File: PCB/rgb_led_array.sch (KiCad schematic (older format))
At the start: 1 part

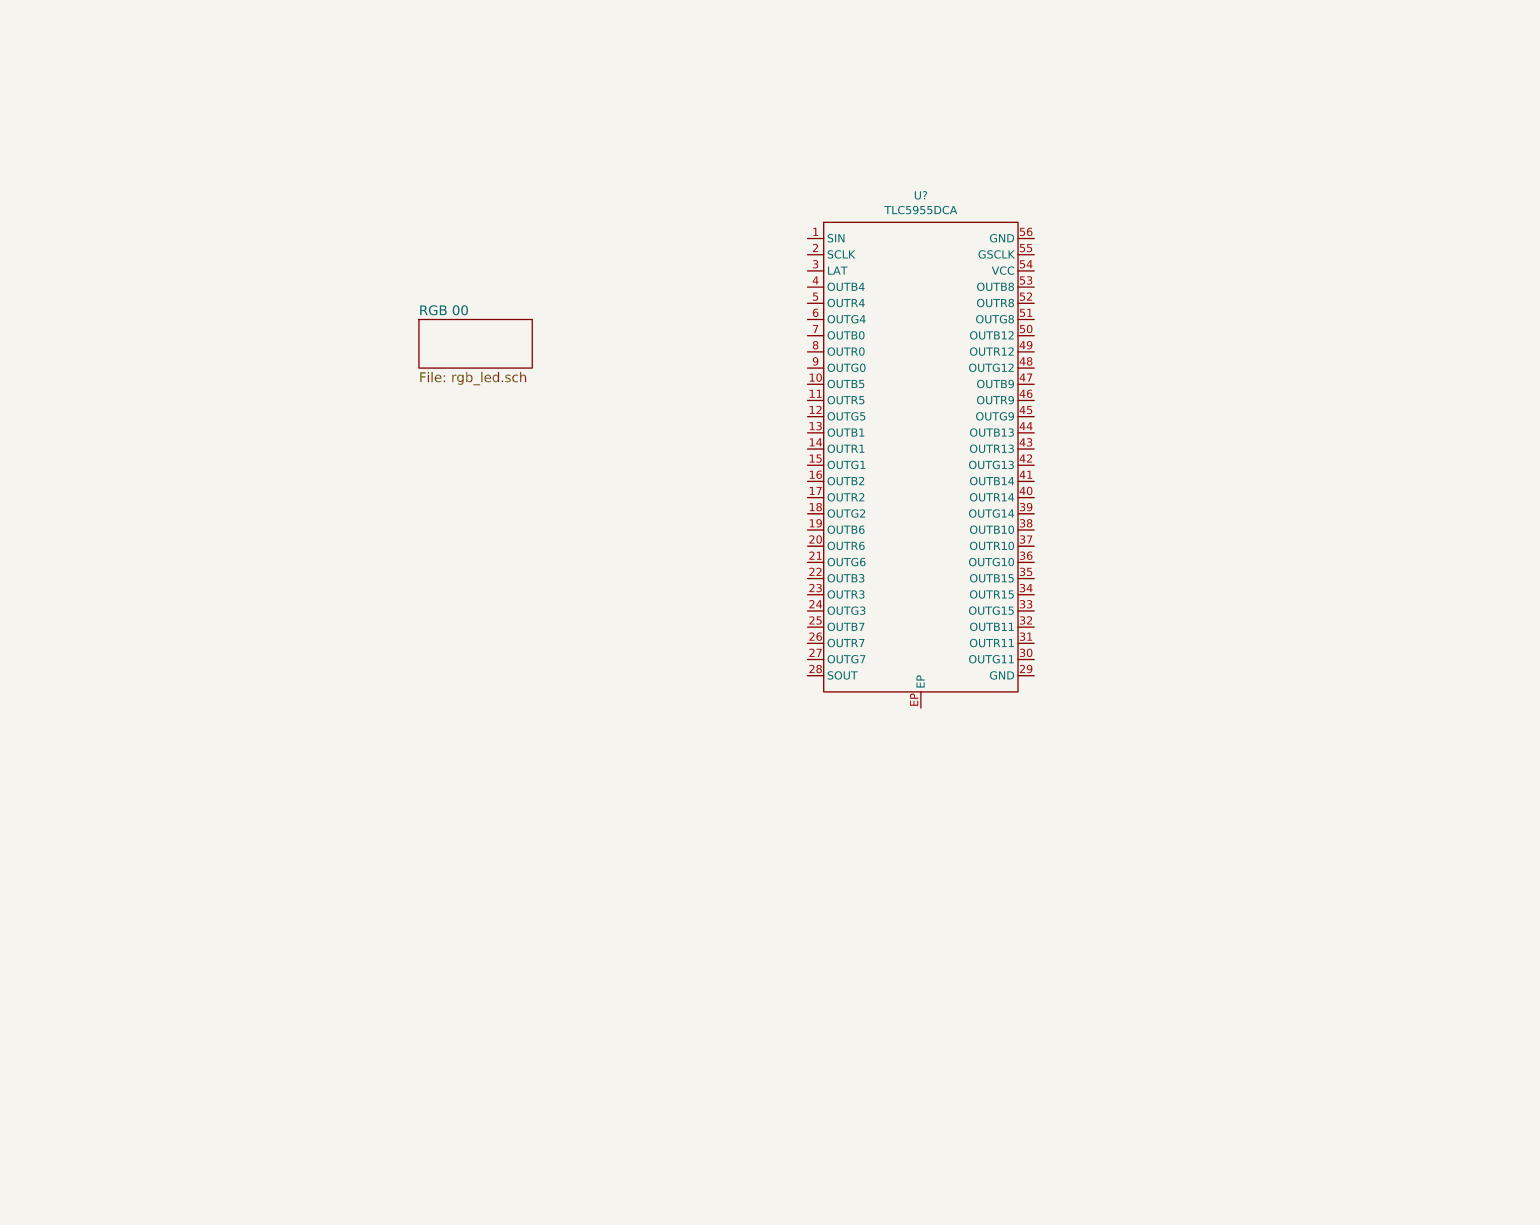
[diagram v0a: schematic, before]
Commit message: PCB Edge.Cuts Defined
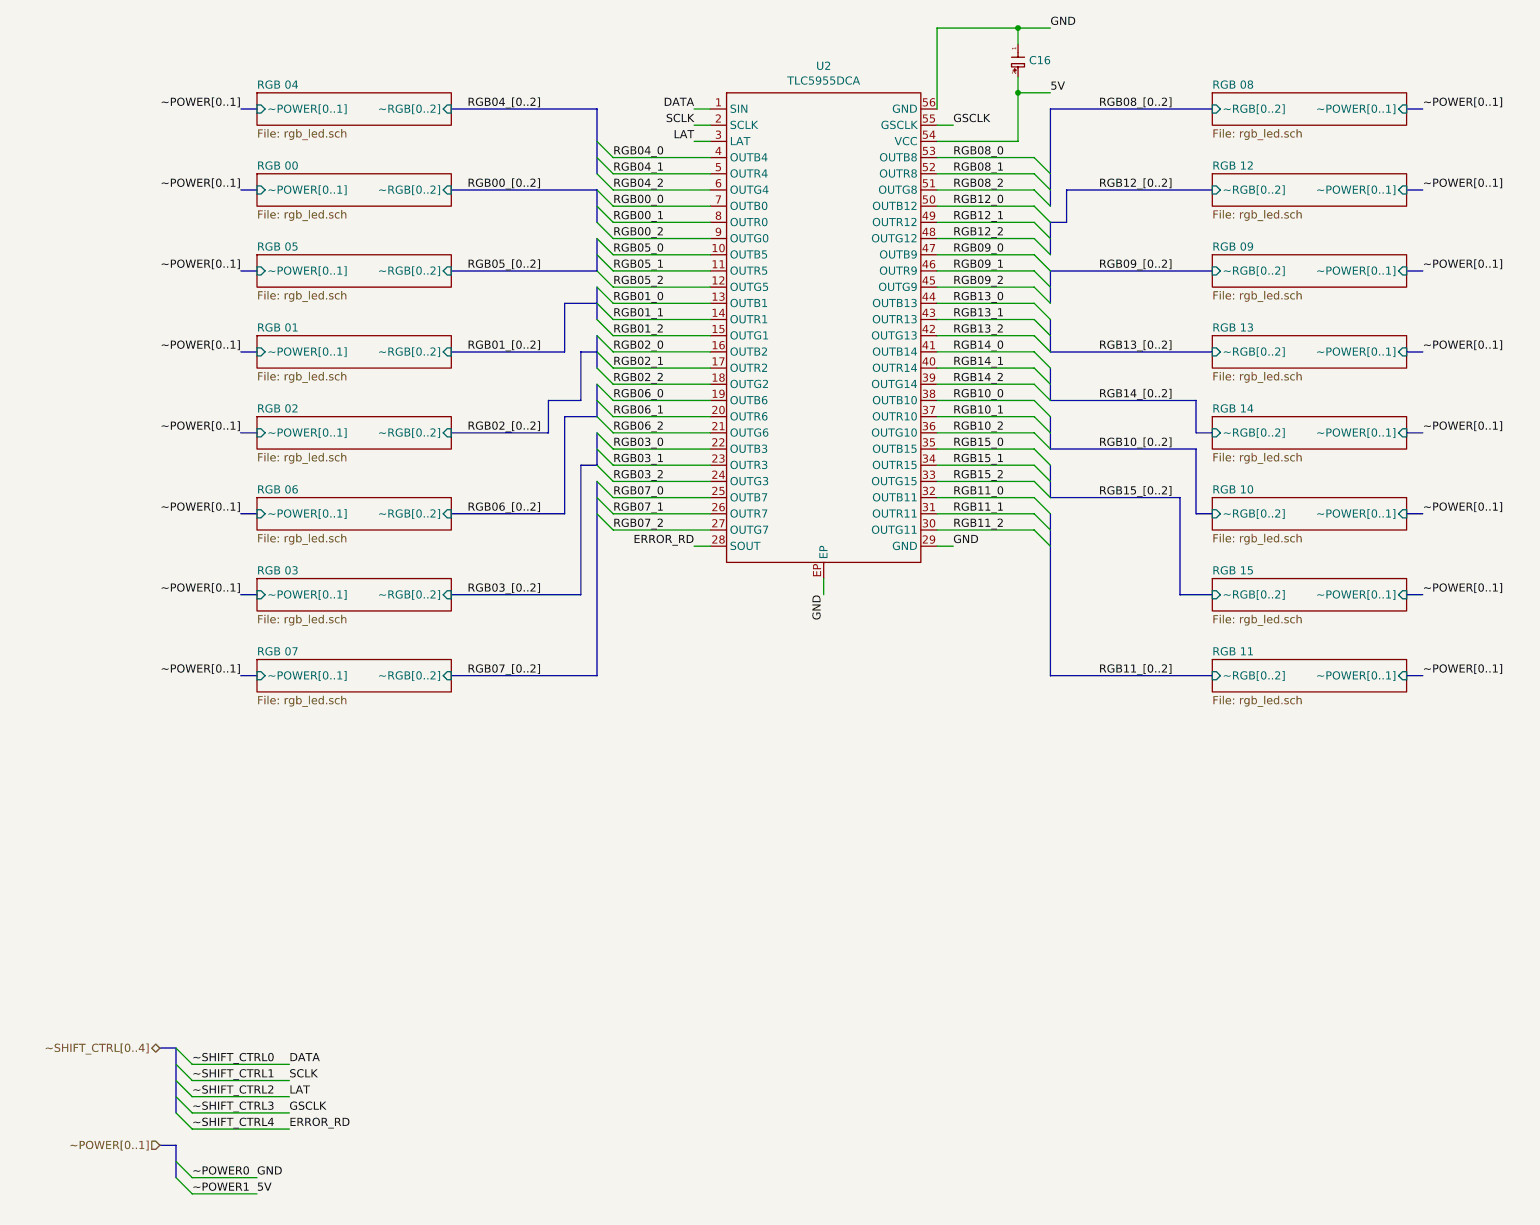
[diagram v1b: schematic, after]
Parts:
- added C16: Capacitor-Pol, local:SMD-POL-1206, symbol Capacitor-Pol
- U2: renamed from U?; footprint (none) -> local:HTSSOP-56_14x6.1; Description (none) -> LED Driver IC 48 Output Linear Analog Dimming 30mA 56-HTSSOP; Included in BOM (none) -> Yes; MPN (none) -> TLC5955DCAR
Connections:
- net DATA: now reaches U2.1 (SIN)
- net RGB05_0: now reaches U2.10 (OUTB5)
- net RGB05_1: now reaches U2.11 (OUTR5)
- net RGB05_2: now reaches U2.12 (OUTG5)
- net RGB01_0: now reaches U2.13 (OUTB1)
- net RGB01_1: now reaches U2.14 (OUTR1)
- net RGB01_2: now reaches U2.15 (OUTG1)
- net RGB02_0: now reaches U2.16 (OUTB2)
- net RGB02_1: now reaches U2.17 (OUTR2)
- net RGB02_2: now reaches U2.18 (OUTG2)
- net RGB06_0: now reaches U2.19 (OUTB6)
- net SCLK: now reaches U2.2 (SCLK)
- net RGB06_1: now reaches U2.20 (OUTR6)
- net RGB06_2: now reaches U2.21 (OUTG6)
- net RGB03_0: now reaches U2.22 (OUTB3)
- net RGB03_1: now reaches U2.23 (OUTR3)
- net RGB03_2: now reaches U2.24 (OUTG3)
- net RGB07_0: now reaches U2.25 (OUTB7)
- net RGB07_1: now reaches U2.26 (OUTR7)
- net RGB07_2: now reaches U2.27 (OUTG7)
- net ERROR_RD: now reaches U2.28 (SOUT)
- net GND: now reaches U2.29 (GND)
- net GND: now also U2.56 (GND), U2.EP, C16.1
- net LAT: now reaches U2.3 (LAT)
- net RGB11_2: now reaches U2.30 (OUTG11)
- net RGB11_1: now reaches U2.31 (OUTR11)
- net RGB11_0: now reaches U2.32 (OUTB11)
- net RGB15_2: now reaches U2.33 (OUTG15)
- net RGB15_1: now reaches U2.34 (OUTR15)
- net RGB15_0: now reaches U2.35 (OUTB15)
- net RGB10_2: now reaches U2.36 (OUTG10)
- net RGB10_1: now reaches U2.37 (OUTR10)
- net RGB10_0: now reaches U2.38 (OUTB10)
- net RGB14_2: now reaches U2.39 (OUTG14)
- net RGB04_0: now reaches U2.4 (OUTB4)
- net RGB14_1: now reaches U2.40 (OUTR14)
- net RGB14_0: now reaches U2.41 (OUTB14)
- net RGB13_2: now reaches U2.42 (OUTG13)
- net RGB13_1: now reaches U2.43 (OUTR13)
- net RGB13_0: now reaches U2.44 (OUTB13)
- net RGB09_2: now reaches U2.45 (OUTG9)
- net RGB09_1: now reaches U2.46 (OUTR9)
- net RGB09_0: now reaches U2.47 (OUTB9)
- net RGB12_2: now reaches U2.48 (OUTG12)
- net RGB12_1: now reaches U2.49 (OUTR12)
- net RGB04_1: now reaches U2.5 (OUTR4)
- net RGB12_0: now reaches U2.50 (OUTB12)
- net RGB08_2: now reaches U2.51 (OUTG8)
- net RGB08_1: now reaches U2.52 (OUTR8)
- net RGB08_0: now reaches U2.53 (OUTB8)
- net 5V: now reaches U2.54 (VCC)
- net 5V: now also C16.2
- net GSCLK: now reaches U2.55 (GSCLK)
- net RGB04_2: now reaches U2.6 (OUTG4)
- net RGB00_0: now reaches U2.7 (OUTB0)
- net RGB00_1: now reaches U2.8 (OUTR0)
- net RGB00_2: now reaches U2.9 (OUTG0)
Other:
- moved on the sheet: U2

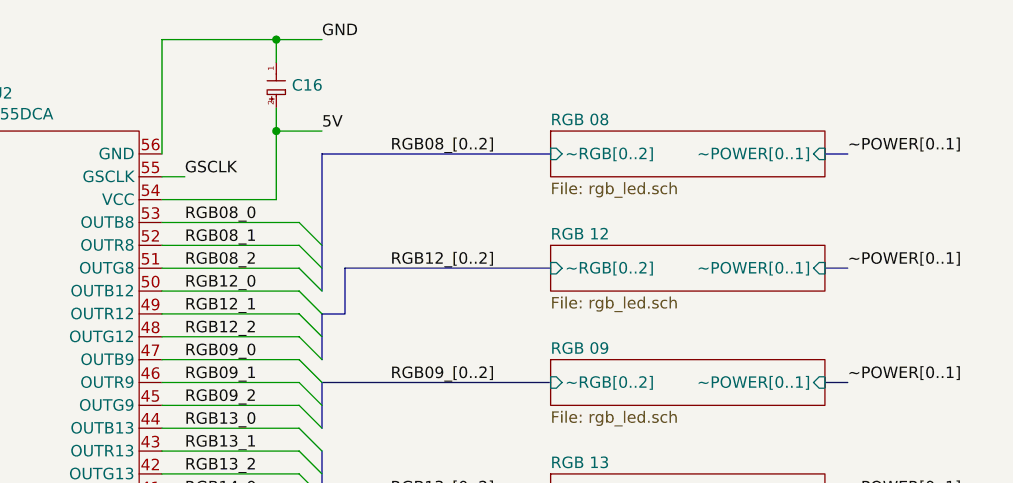
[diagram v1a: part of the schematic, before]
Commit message: Removed extra LED
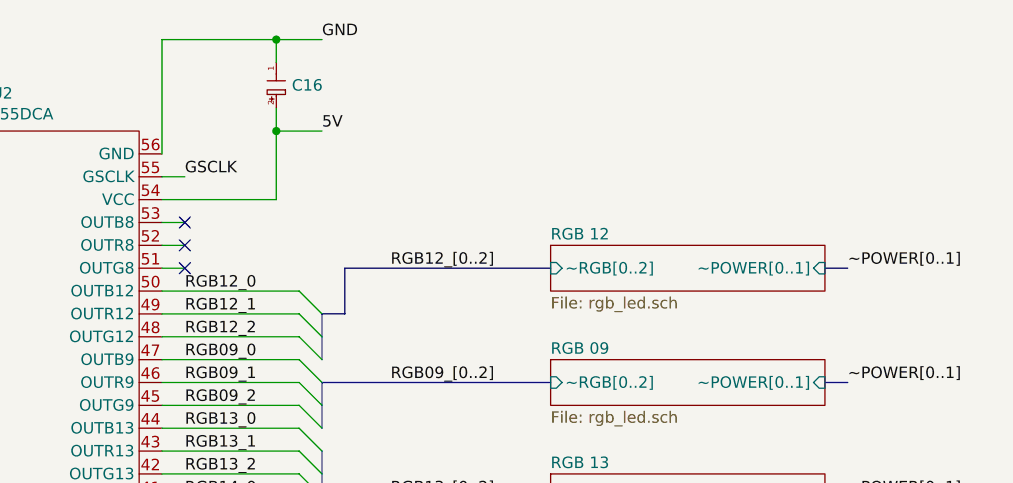
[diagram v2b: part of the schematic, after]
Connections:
- net RGB08_0: no longer names the net of U2.53 (OUTB8)
- net RGB08_1: no longer names the net of U2.52 (OUTR8)
- net RGB08_2: no longer names the net of U2.51 (OUTG8)
- no-connect marks 0 -> 3
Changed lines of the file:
@@
 $Descr A 11000 8500
 encoding utf-8
-Sheet 4 20
+Sheet 4 19
 Title "Christmas Tree Disco"
 Date "2017-08-01"
@@
 F2 "~~RGB[0..2]" I R 3100 4600 50
 F3 "~~POWER[0..1]" I L 1900 4600 50
-$EndSheet
-$Sheet
-S 7800 1000 1200 200
-U 59817080
-F0 "RGB 08" 50
-F1 "rgb_led.sch" 50
-F2 "~~RGB[0..2]" I L 7800 1100 50
-F3 "~~POWER[0..1]" I R 9000 1100 50
 $EndSheet
 Wire Bus Line
@@
 	6100 1900 6700 1900
 Wire Wire Line
-	6100 1400 6700 1400
-Wire Wire Line
-	6100 1500 6700 1500
-Wire Wire Line
-	6100 1600 6700 1600
-Wire Wire Line
 	6100 2000 6700 2000
 Wire Wire Line
@@
 	6100 3700 6700 3700
 Entry Wire Line
-	6700 1400 6800 1500
-Entry Wire Line
-	6700 1500 6800 1600
-Entry Wire Line
-	6700 1600 6800 1700
-Entry Wire Line
 	6700 1700 6800 1800
 Entry Wire Line
@@
 	6700 3700 6800 3800
 Wire Bus Line
-	6800 1100 6800 1700
-Wire Bus Line
 	6800 1800 6800 2000
 Wire Bus Line
@@
 Wire Bus Line
 	6800 3600 6800 4600
-Wire Bus Line
-	7800 1100 6800 1100
 $Sheet
 S 7800 1500 1200 200
@@
 Wire Bus Line
 	6800 4600 7800 4600
-Text Label 6200 1400 0    50   ~ 0
-RGB08_0
-Text Label 6200 1500 0    50   ~ 0
-RGB08_1
-Text Label 6200 1600 0    50   ~ 0
-RGB08_2
 Text Label 6200 1700 0    50   ~ 0
 RGB12_0
@@
 Text Label 6200 3700 0    50   ~ 0
 RGB11_2
-Text Label 7100 1100 0    50   ~ 0
-RGB08_[0..2]
 Text Label 7100 1600 0    50   ~ 0
 RGB12_[0..2]
@@
 Text Label 1800 1100 2    50   ~ 0
 ~~POWER[0..1]
-Text Label 9100 1100 0    50   ~ 0
-~~POWER[0..1]
 Text Label 9100 1600 0    50   ~ 0
 ~~POWER[0..1]
@@
 Wire Bus Line
 	9000 1600 9100 1600
-Wire Bus Line
-	9000 1100 9100 1100
+Wire Wire Line
+	6100 1400 6200 1400
+Wire Wire Line
+	6100 1500 6200 1500
+Wire Wire Line
+	6100 1600 6200 1600
+NoConn ~ 6200 1400
+NoConn ~ 6200 1500
+NoConn ~ 6200 1600
 $EndSCHEMATC

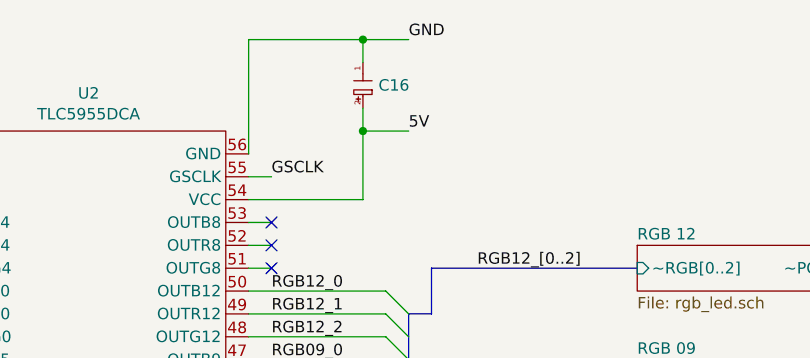
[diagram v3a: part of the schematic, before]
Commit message: PCB Layout
TODO: Change pinouts on dev kit to be compatable with Capacitive Touch
Audio booster pack.
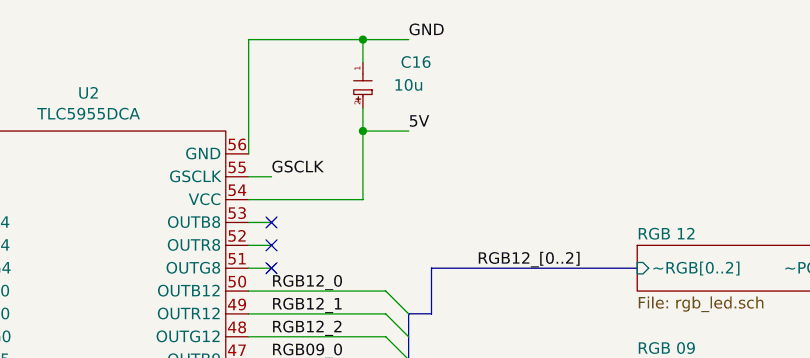
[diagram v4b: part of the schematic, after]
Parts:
- C16: value Capacitor-Pol -> 10u; Description ? -> CAP TANT 10UF 10V 10% 1206; MPN ? -> F931A106KAA
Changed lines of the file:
@@
 Text Label 7100 4600 0    50   ~ 0
 RGB11_[0..2]
-$Comp
-L Capacitor-Pol C16
-U 1 1 59833E85
-P 6600 800
-F 0 "C16" V 6600 868 50  0000 L CNN
-F 1 "Capacitor-Pol" H 6600 960 50  0001 C CNN
-F 2 "local:SMD-POL-1206" H 6600 800 60  0001 C CNN
-F 3 "" H 6600 800 60  0001 C CNN
-F 4 "?" H 6600 800 60  0001 C CNN "MPN"
-F 5 "?" H 6600 800 60  0001 C CNN "Description"
-F 6 "Yes" H 6600 800 60  0001 C CNN "Included in BOM"
-	1    6600 800
-	0    1    1    0
-$EndComp
 Wire Wire Line
 	6600 1300 6100 1300
@@
 NoConn ~ 6200 1500
 NoConn ~ 6200 1600
+$Comp
+L Capacitor-Pol C16
+U 1 1 59893C97
+P 6600 800
+F 0 "C16" V 6500 1100 50  0000 R CNN
+F 1 "10u" V 6600 1000 50  0000 C CNN
+F 2 "local:SMD-POL-1206" H 6600 800 60  0001 C CNN
+F 3 "http://datasheets.avx.com/F93.pdf" H 6600 800 60  0001 C CNN
+F 4 "F931A106KAA" H 6600 800 60  0001 C CNN "MPN"
+F 5 "CAP TANT 10UF 10V 10% 1206" H 6600 800 60  0001 C CNN "Description"
+F 6 "Yes" H 6600 800 60  0001 C CNN "Included in BOM"
+	1    6600 800
+	0    1    1    0
+$EndComp
 $EndSCHEMATC
